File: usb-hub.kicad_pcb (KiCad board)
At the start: 4 copper layers, 50 x 140 mm, 154 parts, among them IC101 USB2517, J101 Barrel_Jack_Switch, J102 USB_C_Receptacle_USB2.0_14P, J201 USB_A, J202 USB_A, J301 USB_A, J302 USB_A, J401 USB_A, J402 USB_A, J601 Prog, SW201 SW_Push, SW202 SW_Push, SW301 SW_Push, SW302 SW_Push, SW401 SW_Push, SW402 SW_Push, U101 USBLC6-2P6, U201 USBLC6-2P6, U202 MIC2026-1xM, U203 USBLC6-2P6, U204 74LVC2G08, U301 USBLC6-2P6, U302 MIC2026-1xM, U303 USBLC6-2P6, U304 74LVC2G08, U401 USBLC6-2P6, U402 MIC2026-1xM, U403 USBLC6-2P6, U404 74LVC2G08, U501 TPS54331, U502 TPS54331, U601 STM32L151C8Tx, Y101 24Mhz

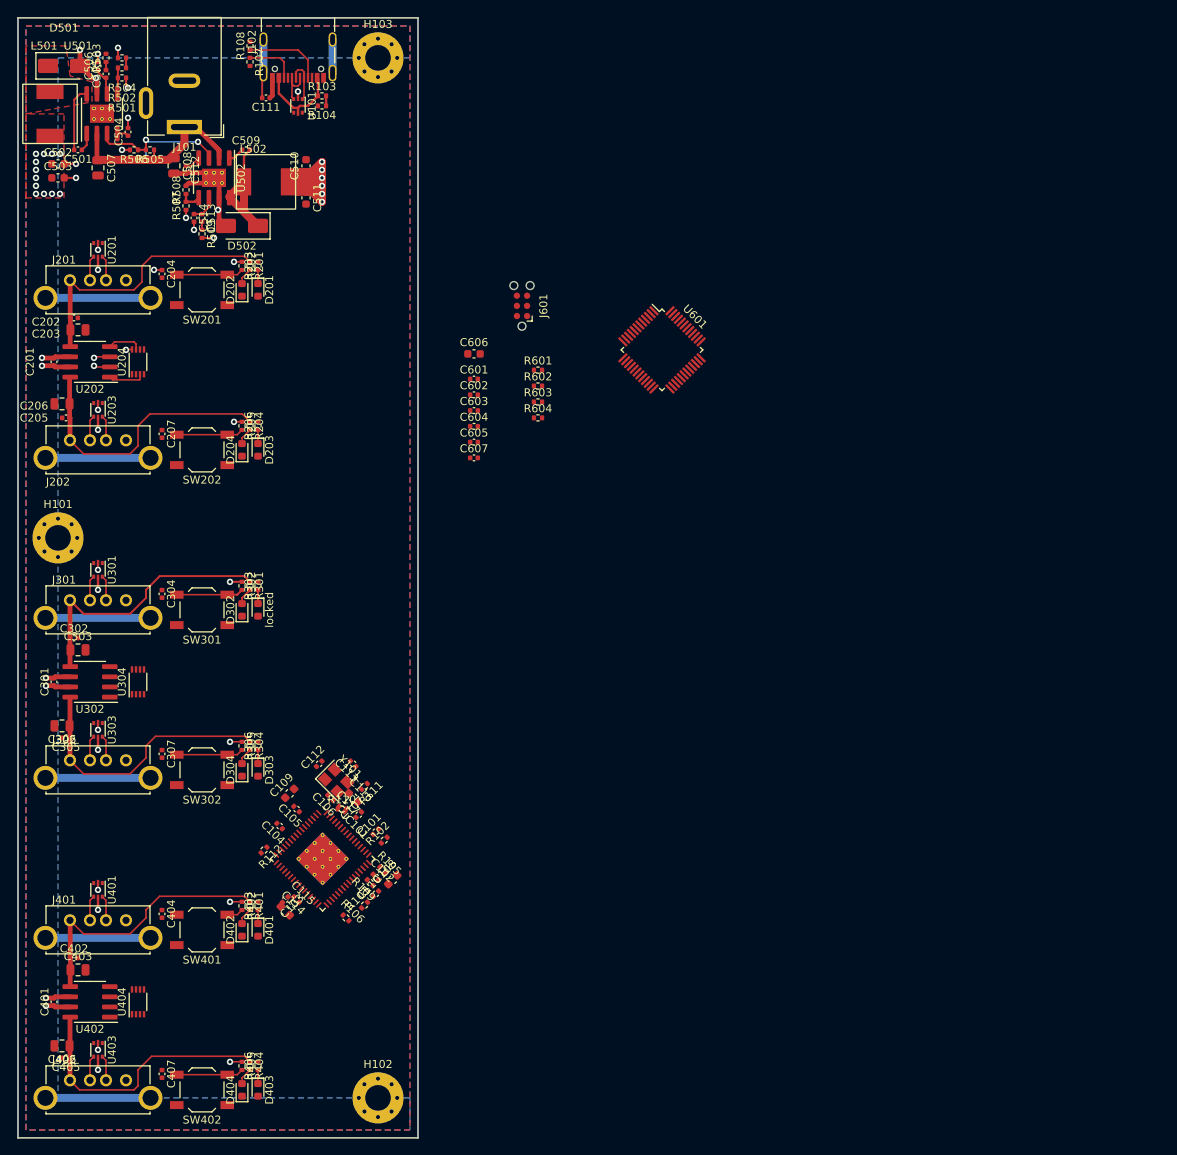
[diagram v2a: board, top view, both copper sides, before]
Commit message: Finish first routing
Routed everything, so that the DRC and ERC do not show anything.
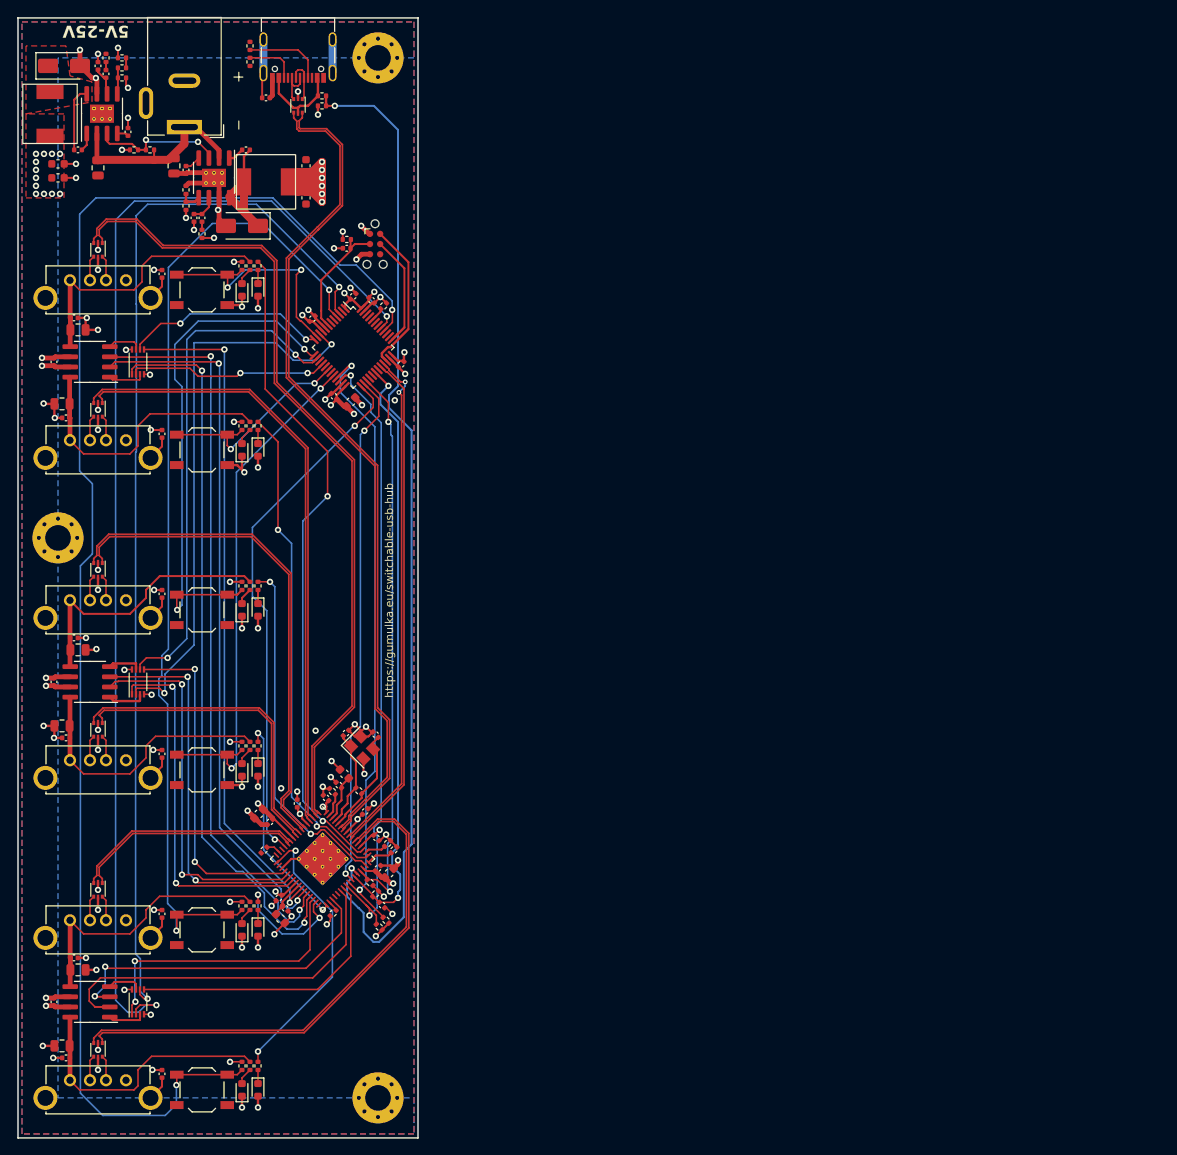
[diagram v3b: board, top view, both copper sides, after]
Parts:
- moved R602 69.4 mm to (146.0, 147.8), turned to 135 degrees
- moved R603 68.6 mm to (145.2, 148.6), turned to 135 degrees
- moved U601 38.6 mm to (141.9, 76.2)
- moved R604 32.7 mm to (141.1, 62.7)
- moved C607 30.7 mm to (141.1, 63.8), turned to 180 degrees
- moved C605 25.4 mm to (136.8, 72.6), turned to 45 degrees
- moved R601 20.9 mm to (145.7, 71.0), turned to 45 degrees
- moved C603 20.8 mm to (141.9, 69.8), turned to 45 degrees
- moved J601 19.9 mm to (144.6, 63.3), turned to -90 degrees
- moved C604 17.9 mm to (139.5, 82.3), turned to 135 degrees
- moved C602 17.4 mm to (144.2, 70.3), turned to -45 degrees
- moved C606 16.5 mm to (141.6, 83.0), turned to 45 degrees
- moved C601 9.29 mm to (147.9, 78.3), turned to -135 degrees
- moved Y101 5.27 mm to (143.0, 126.2)
- moved C112 5.10 mm to (141.0, 124.4)
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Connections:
- net /Power controller/USB_DM renamed /Power controller/USB_D-
- net /Power controller/USB_DP renamed /Power controller/USB_D+
- U601 pad 10: /Port 1-2/PORT_A_EN_2 -> /Port 3-4/PORT_A_EN_2
- U601 pad 12: unconnected-(U601-PA2-Pad12) -> /Port 1-2/PORT_B_EN_2
- U601 pad 13: /Port 1-2/PORT_B_EN_2 -> /Port 3-4/PORT_A_REQ
- U601 pad 14: /Port 1-2/PORT_B_REQ -> /Port 3-4/PORT_B_EN_2
- U601 pad 16: /Port 3-4/PORT_A_EN_2 -> /Port 1-2/PORT_A_EN_2
- U601 pad 17: /Port 3-4/PORT_A_REQ -> unconnected-(U601-PA7-Pad17)
- U601 pad 18: /CFG_SEL1 -> /Port 1-2/PORT_B_REQ
- U601 pad 19: /CFG_SEL2 -> unconnected-(U601-PB1-Pad19)
- U601 pad 20: /SUSP_IND -> /Port 3-4/PORT_B_REQ
- U601 pad 25: unconnected-(U601-PB12-Pad25) -> /CFG_SEL2
- U601 pad 26: /Port 5-6/PORT_B_EN_2 -> /CFG_SEL1
- U601 pad 27: /Port 5-6/PORT_B_REQ -> /SUSP_IND
- U601 pad 3: /Port 3-4/PORT_B_EN_2 -> /Port 5-6/PORT_B_EN_2
- U601 pad 4: /Port 3-4/PORT_B_REQ -> /Port 5-6/PORT_A_REQ
- U601 pad 40: /Port 5-6/PORT_A_EN_2 -> /Port 5-6/PORT_B_REQ
- U601 pad 41: /Port 5-6/PORT_A_REQ -> /Port 5-6/PORT_A_EN_2
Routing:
- net /Port 5-6/PORT_B_REQ: track 8.39 -> 186.5 mm, vias 0 -> 2
- net /Port 5-6/PORT_A_EN_2: track 0.00 -> 149.7 mm, vias 0 -> 2
- net /Port 5-6/PORT_B_EN_2: track 0.00 -> 134.4 mm, vias 0 -> 2
- net /VBUS_DET: track 1.25 -> 128.8 mm, vias 0 -> 2
- net /Port 5-6/PORT_A_REQ: track 2.09 -> 124.3 mm, vias 0 -> 2
- net /USB_UP_D-: track 0.00 -> 104.3 mm
- net /USB_UP_D+: track 0.00 -> 104.1 mm
- net /Port 1-2/USB_A_D-: track 0.00 -> 102.5 mm
- net /Port 1-2/USB_A_D+: track 0.00 -> 101.8 mm
- net GND: track 50.0 -> 149.7 mm, vias 22 -> 76
- net Earth: track 11.6 -> 109.1 mm
- net /Port 1-2/PORT_A_EN_1: track 0.00 -> 90.7 mm, vias 0 -> 2
- net /Port 1-2/PORT_A_OC: track 2.03 -> 92.3 mm, vias 1 -> 2
- net /Port 1-2/PORT_B_OC: track 2.03 -> 89.0 mm, vias 1 -> 2
- net /Port 1-2/PORT_B_EN_1: track 0.00 -> 85.0 mm, vias 0 -> 2
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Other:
- board text added: "5V-25V"
- board text added: "Fabian Pflug USB-Hub ${version}"
- board text added: "https://gumulka.eu/switchable-usb-hub"

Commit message: Improve routing
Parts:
- added REF**: OSHW-Logo2_9.8x8mm_Copper, Symbol:OSHW-Logo2_9.8x8mm_Copper, F.Cu at (143.6, 161.7)
- added REF**: Symbol_Barrel_Polarity, Symbol:Symbol_Barrel_Polarity, F.Cu at (127.5, 45.4)
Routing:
- net /Port 5-6/PORT_A_REQ: track 124.3 -> 115.0 mm
- net /Port 5-6/PORT_B_EN_2: track 134.4 -> 125.5 mm
- net /Port 5-6/PORT_A_EN_2: track 149.7 -> 141.7 mm
- net /Port 5-6/PORT_B_REQ: track 186.5 -> 180.4 mm
- net /Power controller/USB_D-: track 62.9 -> 65.8 mm
- net /Port 3-4/PORT_A_REQ: track 64.5 -> 62.7 mm
- net /Port 3-4/PORT_B_EN_2: track 63.8 -> 62.6 mm
- net /Power/3.5-28V: track 24.9 -> 25.9 mm
- net /Port 1-2/PORT_A_OC: track 92.3 -> 93.0 mm
- net GND: track 149.7 -> 150.2 mm, vias 76 -> 116
- net /RESET_N: track 75.6 -> 75.1 mm

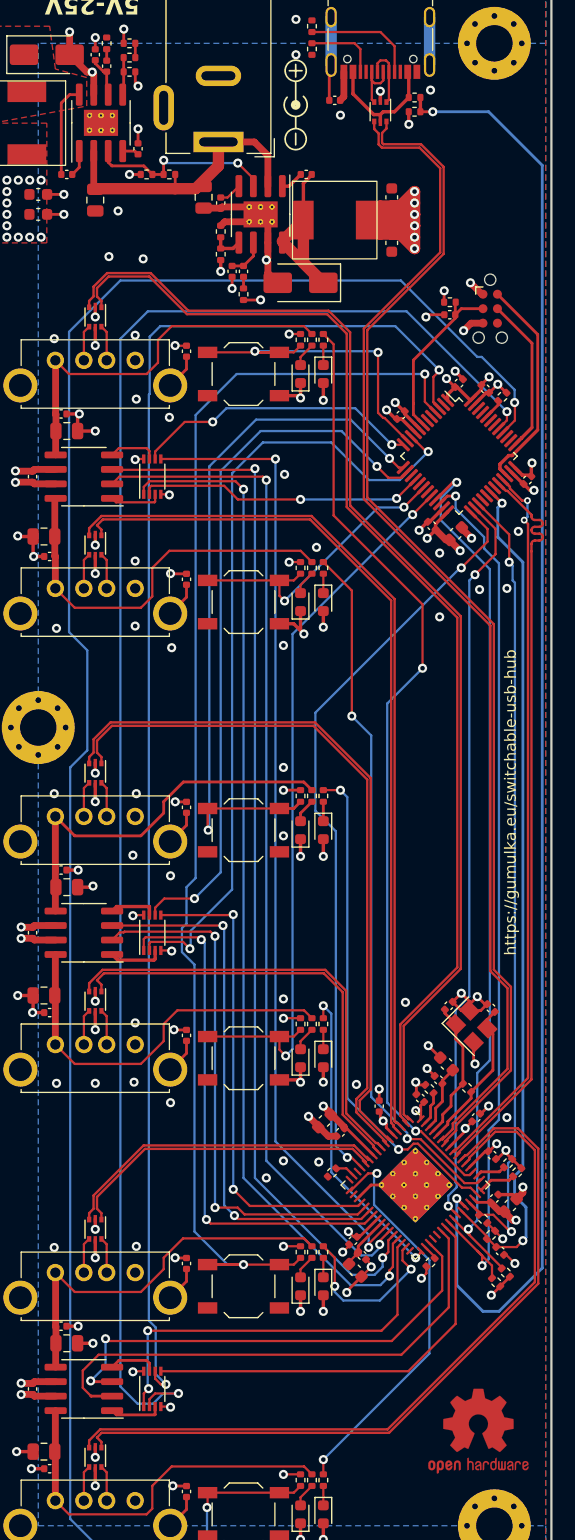
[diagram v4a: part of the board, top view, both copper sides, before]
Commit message: Update to new enviroment
Kicad 8 & global symbols and footprint library
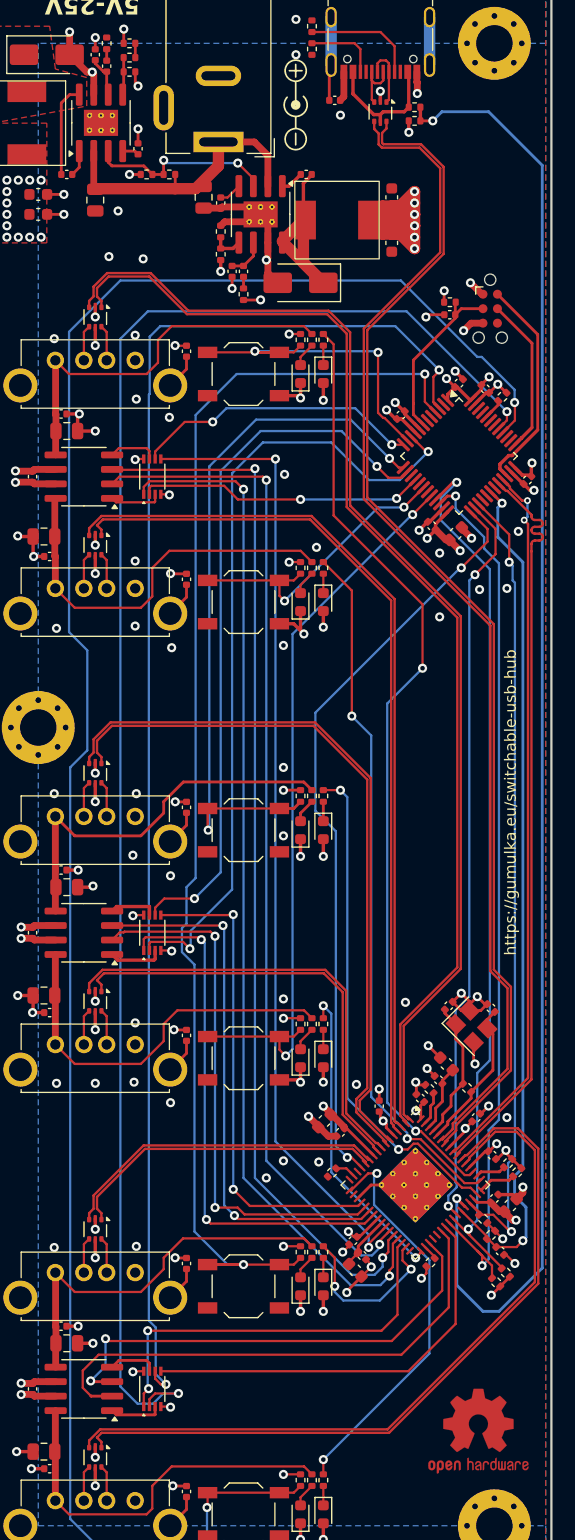
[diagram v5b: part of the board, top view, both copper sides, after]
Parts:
- J201, J202, J301, J302, J401, J402: footprint Connectors:UJ2-AV-W4-TH -> g-Connector_USB:UJ2-AV-W4-TH
- L501, L502: footprint Inductors:YSPI0630A -> g-Inductors:YSPI0630A
- moved R103 0.85 mm to (138.0, 45.6)
- moved R104 0.80 mm to (138.0, 46.8)
- moved L502 0.20 mm to (131.2, 55.5)
- renumbered locked to D301
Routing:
- net GND: track 150.2 -> 152.0 mm
- net +3V3: track 101.2 -> 100.4 mm
